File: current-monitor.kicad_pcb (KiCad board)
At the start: 4 copper layers, 70 x 60 mm, 152 parts, among them J201 CONN-3, J601 USB-MICROB, J602 SWD, J603 CONN-6, K201 RELAY-DPDT-EE2-SPLIT, K202 RELAY-DPDT-EE2-SPLIT, Q201 DRDC3105E6, U201 FSA1259A, U202 MAX4737EUD, U301 AD8429A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

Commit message: 1.0-rc1
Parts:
- added TP706: GND, libs:TESTPOINT-2.0, F.Cu at (97.4, 114.6)
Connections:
- R605 pad 1: /MCU/LED_ERROR -> /MCU/LED_CAPTURE
- R606 pad 1: /MCU/LED_CAPTURE -> /MCU/LED_CALIBRATE
- R607 pad 1: /MCU/LED_CALIBRATE -> /MCU/LED_ERROR
- U601 pad 53: /MCU/LED_CALIBRATE -> /MCU/LED_ERROR
- U601 pad 54: /MCU/LED_CAPTURE -> /MCU/LED_CALIBRATE
- U601 pad 55: /MCU/LED_ERROR -> /MCU/LED_CAPTURE
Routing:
- net /MCU/LED_ERROR: track 95.4 -> 79.2 mm
- net /MCU/LED_CAPTURE: track 86.6 -> 95.4 mm
- net /MCU/LED_CALIBRATE: track 79.2 -> 86.6 mm
- net COM: track 114.4 -> 116.1 mm, vias 107 -> 108
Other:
- board text added: "CALIBRATE"
- board text added: "CAPTURE"
- board text added: "ERROR"
- board text added: "POWER"
- board text added: "SER#"
- board text added: "v1.0"
- board text removed: "sternlabs"

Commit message: silkscreen
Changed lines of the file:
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@@
   (module libs:SMD-3225 (layer F.Cu)
     (at 142.6 115.4 180)
-    (fp_text reference C713 (at 2 0 270) (layer F.SilkS)
+    (fp_text reference C713 (at 0 -2.8 360) (layer F.SilkS)
       (effects (font (size 0.7 0.7) (thickness 0.15)))
     )
@@
     )
   )
-  (zone (net 2) (net_name COM) (layer F.SilkS) (hatch edge 0.508)
+  (zone (net 0) (net_name "") (layer F.SilkS) (hatch edge 0.508)
     (connect_pads (clearance 0.2))
     (min_thickness 0.254)

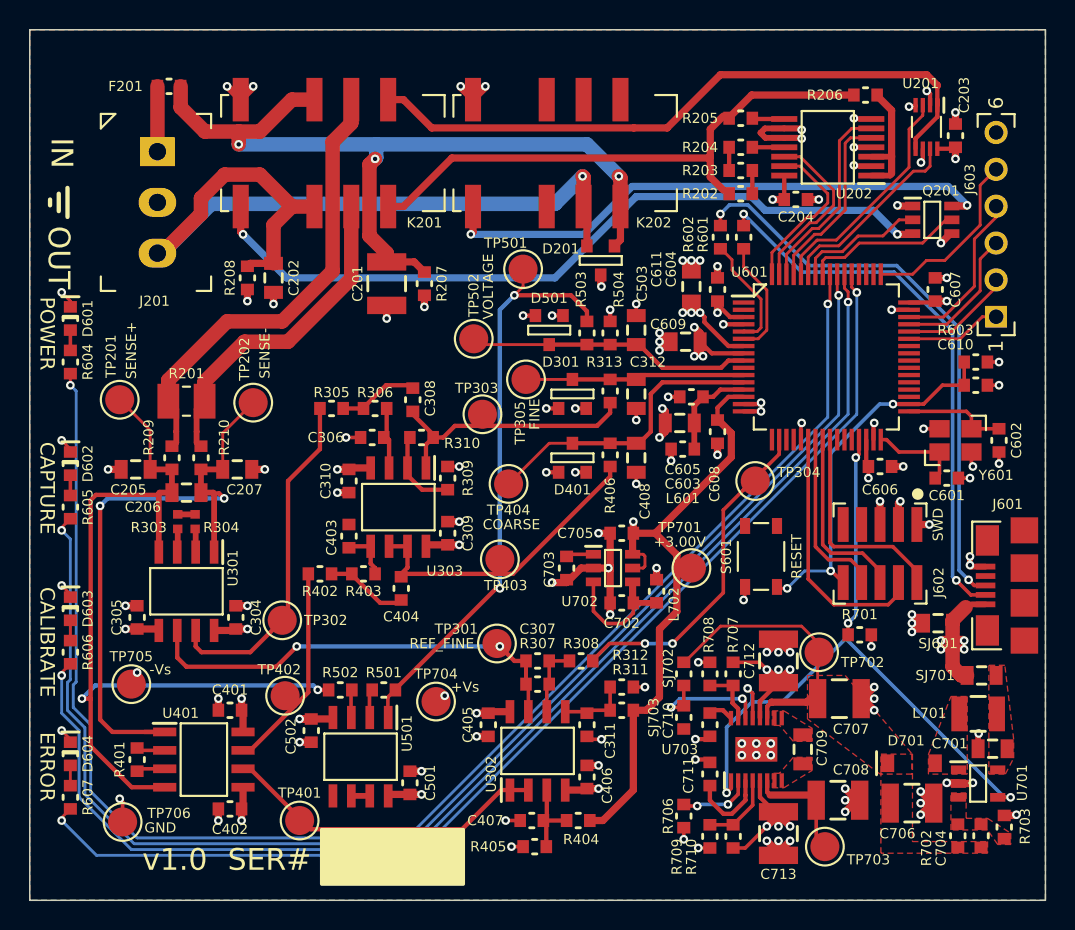
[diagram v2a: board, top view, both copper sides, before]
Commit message: move SJ for mcu
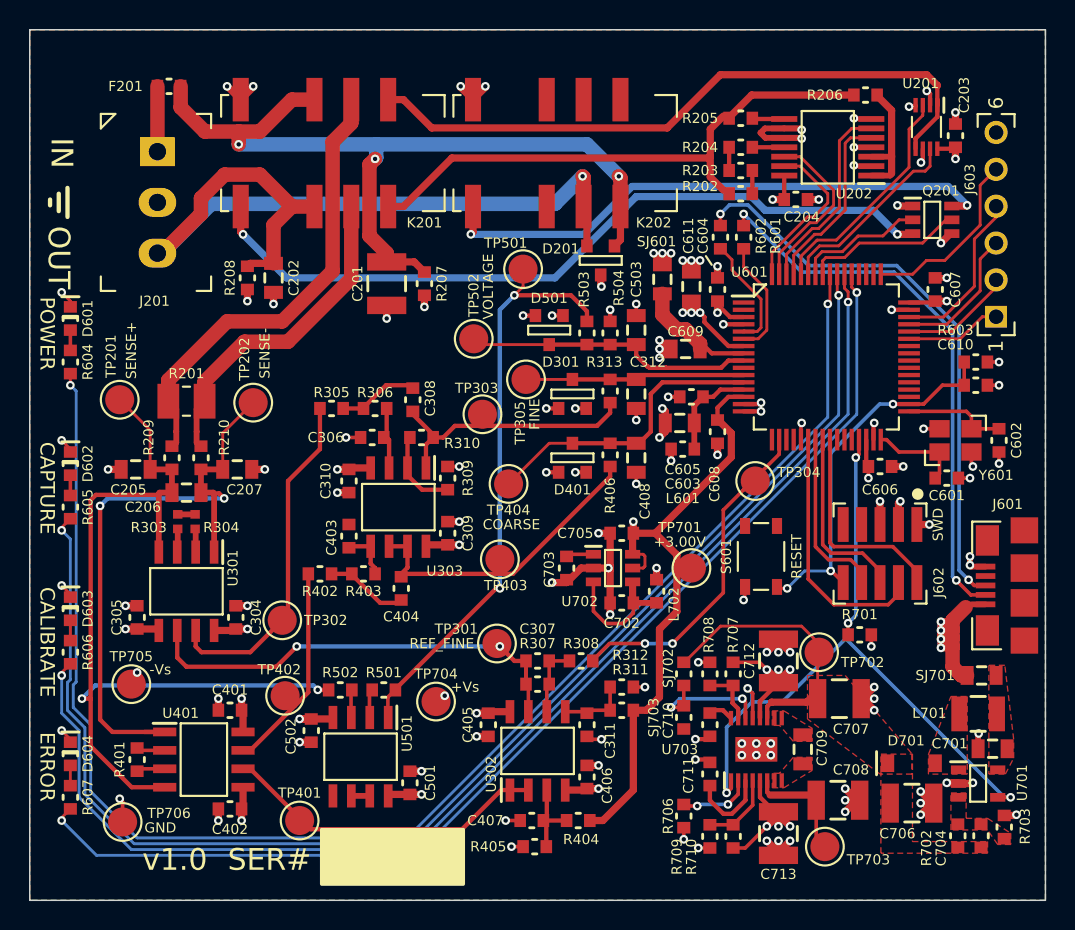
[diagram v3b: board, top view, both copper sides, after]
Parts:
- moved SJ601 30.4 mm to (134.6, 77.2), turned to 0 degrees
- moved C609 0.50 mm to (136.2, 82.0)
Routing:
- net /MCU/5V_MCU: track 34.9 -> 8.56 mm, vias 6 -> 0
- net +5V: track 39.4 -> 47.6 mm, vias 12 -> 15
- net /MCU/SENSE_VOLTAGE: track 21.9 -> 20.5 mm

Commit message: tidy up power plane
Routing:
- net -Vs: track 68.9 -> 45.2 mm
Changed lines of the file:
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@@
     (thickness 1.6)
     (drawings 20)
-    (tracks 1208)
+    (tracks 1206)
     (zones 0)
     (modules 153)
@@
     (trace_clearance 0.199)
     (zone_clearance 0.2)
-    (zone_45_only no)
+    (zone_45_only yes)
     (trace_min 0.15)
     (segment_width 0.15)
@@
   (via (at 97.6 101.3) (size 0.6) (drill 0.3) (layers F.Cu B.Cu) (net 5))
   (segment (start 108.845604 113.750999) (end 106.349001 113.750999) (width 0.5) (layer In2.Cu) (net 5))
-  (segment (start 131.650999 113.750999) (end 108.845604 113.750999) (width 0.5) (layer In2.Cu) (net 5))
   (segment (start 108.845604 113.750999) (end 108.845604 108.254396) (width 0.5) (layer In2.Cu) (net 5))
   (segment (start 108.845604 108.254396) (end 109.6 107.5) (width 0.5) (layer In2.Cu) (net 5))
-  (segment (start 132.292925 114.392925) (end 131.650999 113.750999) (width 0.5) (layer In2.Cu) (net 5))
   (segment (start 106.349001 113.750999) (end 105.6 114.5) (width 0.5) (layer In2.Cu) (net 5))
   (segment (start 141.075109 114.392925) (end 132.292925 114.392925) (width 0.5) (layer In2.Cu) (net 5))
@@
     )
   )
-  (zone (net 5) (net_name -Vs) (layer In2.Cu) (hatch edge 0.508)
+  (zone (net 2) (net_name COM) (layer In1.Cu) (hatch edge 0.508)
     (connect_pads yes (clearance 0.2))
     (min_thickness 0.254)
@@
     (polygon
       (pts
-        (xy 145.8 117.3) (xy 95.6 117.3) (xy 95.6 88.9) (xy 115.8 88.9) (xy 124.2 110.1)
-        (xy 144.4 110.1)
+        (xy 91 60) (xy 161 60) (xy 161 120) (xy 91 120)
       )
     )
   )
-  (zone (net 4) (net_name +Vs) (layer In2.Cu) (hatch edge 0.508)
-    (priority 1)
+  (zone (net 2) (net_name COM) (layer B.Cu) (hatch edge 0.508)
     (connect_pads yes (clearance 0.2))
     (min_thickness 0.254)
@@
     (polygon
       (pts
-        (xy 144.6 102.9) (xy 129 102.9) (xy 122.2 93.1) (xy 115.8 93.1) (xy 102.8 100.5)
-        (xy 103 108.1) (xy 113.2 105.3) (xy 117.2 113.5) (xy 128.4 109.7) (xy 144.6 109.9)
+        (xy 91 60) (xy 161 60) (xy 161 120) (xy 91 120)
       )
     )
   )
-  (zone (net 8) (net_name +5V) (layer In2.Cu) (hatch edge 0.508)
-    (priority 2)
-    (connect_pads yes (clearance 0.2))
+  (zone (net 0) (net_name "") (layer F.SilkS) (hatch edge 0.508)
+    (connect_pads (clearance 0.2))
     (min_thickness 0.254)
-    (fill yes (arc_segments 32) (thermal_gap 0.508) (thermal_bridge_width 0.508))
+    (fill yes (arc_segments 16) (thermal_gap 0.508) (thermal_bridge_width 0.508))
     (polygon
       (pts
-        (xy 133 95.5) (xy 133.2 100.9) (xy 155.2 104.5) (xy 160.4 98.1) (xy 160.4 62.3)
-        (xy 103.2 62.3) (xy 103 74.2) (xy 155 77.7) (xy 155 81.1) (xy 158.8 82.6)
-        (xy 154 96.3)
+        (xy 111 115) (xy 121 115) (xy 121 119) (xy 111 119)
       )
     )
   )
   (zone (net 13) (net_name +3V3) (layer In2.Cu) (hatch edge 0.508)
-    (priority 1)
+    (priority 2)
     (connect_pads yes (clearance 0.2))
     (min_thickness 0.254)
@@
     (polygon
       (pts
-        (xy 159.6 78.5) (xy 159.2 87.5) (xy 153.4 95.2) (xy 137.6 91.7) (xy 126.6 91.9)
-        (xy 123.2 77.2)
+        (xy 123 88.6) (xy 130.2 95.8) (xy 153.2 95.8) (xy 153.2 88.4) (xy 158.8 82.8)
+        (xy 155.2 79.2) (xy 155.2 77.2) (xy 124.6 77.2) (xy 123 78.8)
       )
     )
   )
-  (zone (net 2) (net_name COM) (layer In1.Cu) (hatch edge 0.508)
+  (zone (net 4) (net_name +Vs) (layer In2.Cu) (hatch edge 0.508)
+    (priority 2)
     (connect_pads yes (clearance 0.2))
     (min_thickness 0.254)
@@
     (polygon
       (pts
-        (xy 91 60) (xy 161 60) (xy 161 120) (xy 91 120)
+        (xy 127.8 101.2) (xy 144.2 101.2) (xy 144.2 108.4) (xy 124 108.4) (xy 119 113.4)
+        (xy 117 113.4) (xy 110.4 106.8) (xy 104.8 106.8) (xy 104.8 99.8) (xy 110.2 94.4)
+        (xy 121 94.4) (xy 127.8 101.2)
       )
     )
   )
-  (zone (net 2) (net_name COM) (layer B.Cu) (hatch edge 0.508)
+  (zone (net 5) (net_name -Vs) (layer In2.Cu) (hatch edge 0.508)
+    (priority 1)
     (connect_pads yes (clearance 0.2))
     (min_thickness 0.254)
@@
     (polygon
       (pts
-        (xy 91 60) (xy 161 60) (xy 161 120) (xy 91 120)
+        (xy 134.6 108.4) (xy 144.2 108.4) (xy 144.2 120) (xy 96.6 120) (xy 96.6 88.2)
+        (xy 114.4 88.2) (xy 134.6 108.4)
       )
     )
   )
-  (zone (net 0) (net_name "") (layer F.SilkS) (hatch edge 0.508)
-    (connect_pads (clearance 0.2))
+  (zone (net 8) (net_name +5V) (layer In2.Cu) (hatch edge 0.508)
+    (connect_pads yes (clearance 0.2))
     (min_thickness 0.254)
-    (fill yes (arc_segments 16) (thermal_gap 0.508) (thermal_bridge_width 0.508))
+    (fill yes (arc_segments 32) (thermal_gap 0.508) (thermal_bridge_width 0.508))
     (polygon
       (pts
-        (xy 111 115) (xy 121 115) (xy 121 119) (xy 111 119)
+        (xy 91 120) (xy 91 60) (xy 161 60) (xy 161 120)
       )
     )

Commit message: slight track cleanup
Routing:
- net Net-(K201-Pad12): track 52.8 -> 51.1 mm
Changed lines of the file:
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@@
   (segment (start 138.807125 114.037396) (end 139.39264 114.037396) (width 0.3) (layer F.Cu) (net 42))
   (segment (start 140.325109 113.104927) (end 140.325109 111.742925) (width 0.3) (layer F.Cu) (net 42) (status 20))
-  (segment (start 150.8 74.1) (end 149.149001 72.449001) (width 0.5) (layer B.Cu) (net 43))
-  (segment (start 149.149001 72.449001) (end 141.684295 72.449001) (width 0.5) (layer B.Cu) (net 43))
-  (segment (start 141.684295 72.449001) (end 140.735294 71.5) (width 0.5) (layer B.Cu) (net 43))
-  (segment (start 140.735294 71.5) (end 132.8 71.5) (width 0.5) (layer B.Cu) (net 43))
-  (segment (start 132.8 71.5) (end 127.2 77.1) (width 0.5) (layer B.Cu) (net 43))
-  (segment (start 127.2 77.1) (end 108.7 77.1) (width 0.5) (layer B.Cu) (net 43))
-  (segment (start 108.7 77.1) (end 105.7 74.1) (width 0.5) (layer B.Cu) (net 43))
+  (segment (start 150.8 74.1) (end 143.335294 74.1) (width 0.5) (layer B.Cu) (net 43))
+  (segment (start 140.735294 71.5) (end 136.488548 71.5) (width 0.5) (layer B.Cu) (net 43))
+  (segment (start 143.335294 74.1) (end 140.735294 71.5) (width 0.5) (layer B.Cu) (net 43))
+  (segment (start 136.488548 71.5) (end 132.988548 75) (width 0.5) (layer B.Cu) (net 43))
+  (segment (start 132.988548 75) (end 106.6 75) (width 0.5) (layer B.Cu) (net 43))
+  (segment (start 106.6 75) (end 105.999999 74.399999) (width 0.5) (layer B.Cu) (net 43))
+  (segment (start 105.999999 74.399999) (end 105.7 74.1) (width 0.5) (layer B.Cu) (net 43))
   (segment (start 150.8 74.1) (end 151.8 74.1) (width 0.5) (layer F.Cu) (net 43) (status 20))
   (segment (start 151.8 74.1) (end 151.85 74.05) (width 0.5) (layer F.Cu) (net 43) (status 30))
@@
   (segment (start 105.54 73.94) (end 105.7 74.1) (width 0.5) (layer F.Cu) (net 43))
   (via (at 105.7 74.1) (size 0.6) (drill 0.3) (layers F.Cu B.Cu) (net 43))
-  (segment (start 121.4 74.1) (end 129.211452 74.1) (width 0.5) (layer B.Cu) (net 44))
-  (segment (start 129.211452 74.1) (end 132.510461 70.80099) (width 0.5) (layer B.Cu) (net 44))
-  (segment (start 132.510461 70.80099) (end 154.30099 70.80099) (width 0.5) (layer B.Cu) (net 44))
   (segment (start 154.30099 70.80099) (end 155.6 72.1) (width 0.5) (layer B.Cu) (net 44))
+  (segment (start 121.4 74.1) (end 132.9 74.1) (width 0.5) (layer B.Cu) (net 44))
+  (segment (start 132.9 74.1) (end 136.19901 70.80099) (width 0.5) (layer B.Cu) (net 44))
+  (segment (start 136.19901 70.80099) (end 154.30099 70.80099) (width 0.5) (layer B.Cu) (net 44))
   (segment (start 121.55 72.183) (end 121.55 73.95) (width 0.5) (layer F.Cu) (net 44) (status 10))
   (segment (start 121.55 73.95) (end 121.4 74.1) (width 0.5) (layer F.Cu) (net 44))

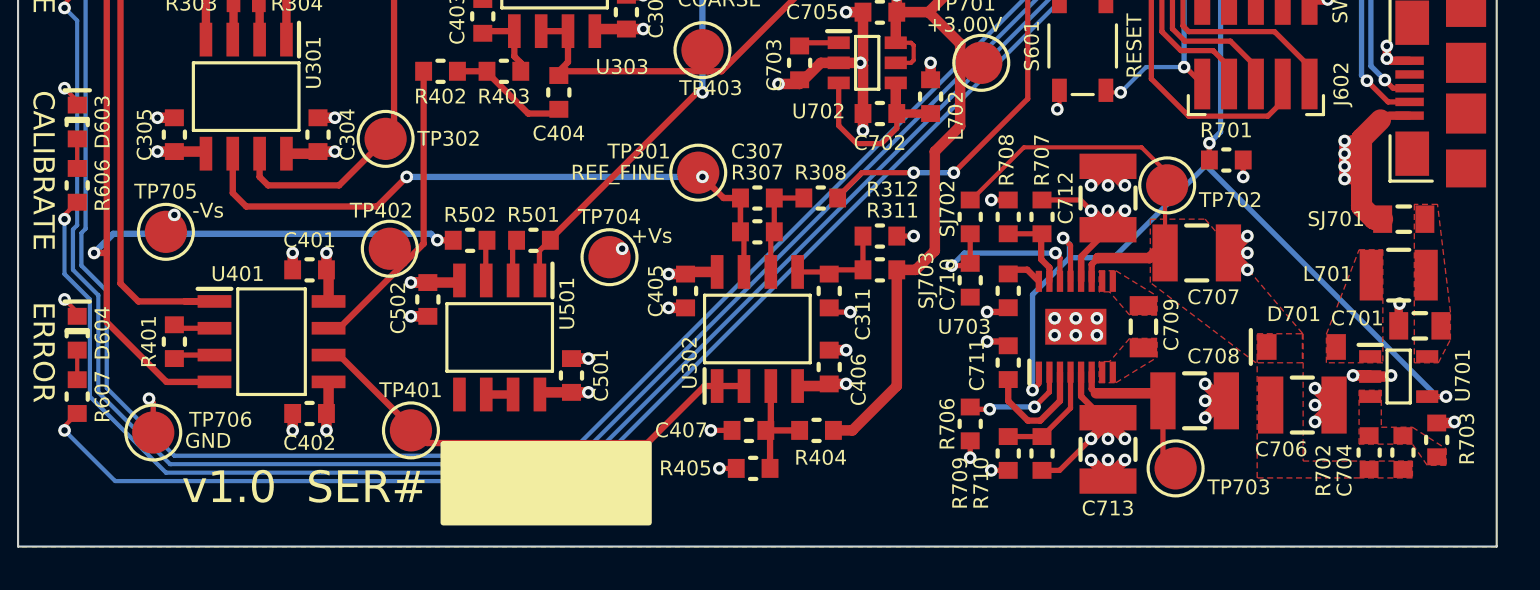
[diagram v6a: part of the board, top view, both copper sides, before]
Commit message: change power supply
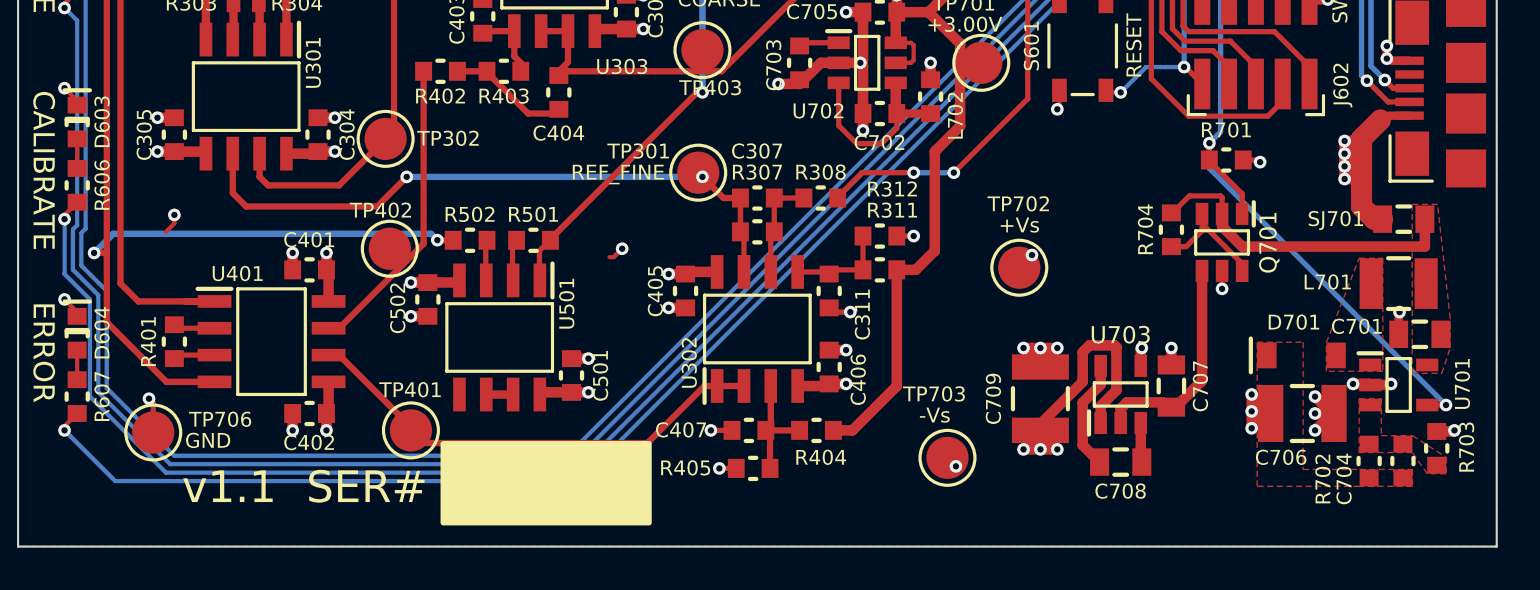
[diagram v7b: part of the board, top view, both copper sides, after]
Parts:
- removed C710, C711: 10n, libs:SMD-1608
- removed C712, C713: 10u, libs:SMD-3225
- removed R706, SJ702, SJ703: 0, libs:SMD-1608
- removed R707, R710: 1.15M, libs:SMD-1608
- removed R708, R709: 100k, libs:SMD-1608
- removed TP704: +Vs, libs:TESTPOINT-2.0
- removed TP705: -Vs, libs:TESTPOINT-2.0
- added Q701: DMG6601LVT, libs:SOT-23-6, F.Cu at (148.0, 105.6)
- added R704: 51k, libs:SMD-1608, F.Cu at (145.6, 105.0)
- C704: value 120p -> 134p
- C707, C708: value 10u -> 2.2u; footprint libs:SMD-3225 -> libs:SMD-2012
- C709: value 2.2u -> 10u; footprint libs:SMD-2012 -> libs:SMD-3225
- R702: value 174k -> 149k
- TP702: value +Vs_UNREG -> +Vs
- TP703: value -Vs_UNREG -> -Vs
- U703: value LTC3260MSE -> TPS6040x; footprint libs:MSOP-16-EP -> libs:SOT-23-5
- moved TP703 10.8 mm to (135.0, 115.8)
- moved TP702 8.01 mm to (138.4, 106.8)
- moved C707 6.41 mm to (145.6, 112.4), turned to 180 degrees
- moved C709 5.95 mm to (139.4, 113.0), turned to 180 degrees
- moved C708 4.55 mm to (143.2, 116.0), turned to 270 degrees
- moved U703 3.85 mm to (143.2, 112.8)
- moved C701 0.40 mm to (157.4, 110.0)
- moved C704 0.40 mm to (156.6, 116.0)
- moved C706 0.40 mm to (151.8, 113.7)
- moved D701 0.40 mm to (151.8, 111.0)
- moved R702 0.40 mm to (155.0, 116.0)
- moved L701 0.40 mm to (156.4, 107.6)
- moved R703 0.40 mm to (158.2, 115.4)
- moved U701 0.40 mm to (156.4, 112.4)
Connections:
- C704 pad 1: /Power Supply/+Vs_UNREG -> +Vs
- C706 pad 1: /Power Supply/+Vs_UNREG -> +Vs
- C707 pad 1: /Power Supply/+Vs_UNREG -> Net-(C707-Pad1)
- C708 pad 1: /Power Supply/-Vs_UNREG -> Net-(C708-Pad1)
- C708 pad 2: COM -> Net-(C708-Pad2)
- C709 pad 1: /Power Supply/PUMP+ -> -Vs
- C709 pad 2: /Power Supply/PUMP- -> COM
- D701 pad C: /Power Supply/+Vs_UNREG -> +Vs
- R702 pad 1: /Power Supply/+Vs_UNREG -> +Vs
- TP702 pad TP: /Power Supply/+Vs_UNREG -> +Vs
- TP703 pad TP: /Power Supply/-Vs_UNREG -> -Vs
- U703 pad 1: /MCU/VS_ENABLE -> -Vs
- U703 pad 2: Net-(R706-Pad1) -> Net-(C707-Pad1)
- U703 pad 3: Net-(C711-Pad2) -> Net-(C708-Pad1)
- U703 pad 4: Net-(R709-Pad2) -> COM
- U703 pad 5: -Vs -> Net-(C708-Pad2)
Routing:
- net /Power Supply/+Vs_UNREG: track 19.1 -> 0.00 mm
- net COM: track 116.2 -> 99.1 mm, vias 108 -> 91
- net /MCU/VS_ENABLE: track 51.2 -> 34.9 mm, vias 5 -> 3
- net /Power Supply/5V_ANALOG: track 0.09 -> 15.5 mm
- net Net-(C707-Pad1): track 0.00 -> 10.5 mm
- net Net-(SJ702-Pad1): track 8.90 -> 0.00 mm, vias 2 -> 0
- net /Power Supply/-Vs_UNREG: track 7.90 -> 0.00 mm
- net Net-(Q701-Pad3): track 0.00 -> 6.05 mm
- net Net-(C711-Pad2): track 5.40 -> 0.00 mm
- net Net-(R709-Pad2): track 5.28 -> 0.00 mm
- net Net-(C708-Pad2): track 0.00 -> 5.23 mm
- net Net-(R706-Pad1): track 5.20 -> 0.00 mm, vias 2 -> 0
- net -Vs: track 45.2 -> 49.9 mm
- net +Vs: track 83.8 -> 79.2 mm
- net Net-(R707-Pad2): track 4.10 -> 0.00 mm
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- added copper zone on F.Cu, net +Vs
- removed copper zone on F.Cu, net /Power Supply/+Vs_UNREG
- removed copper zone on F.Cu, net /Power Supply/PUMP+
- removed copper zone on F.Cu, net /Power Supply/PUMP-
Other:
- board text added: "v1.1"
- board text removed: "v1.0"

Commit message: pcb cleanup
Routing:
- net (no net): track 1.73 -> 0.97 mm, vias 2 -> 1
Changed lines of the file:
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@@
     (links 311)
     (no_connects 0)
-    (area 90.949999 59.949999 161.050001 120.050001)
+    (area 90.949999 59.949999 162.774001 120.050001)
     (thickness 1.6)
     (drawings 20)
-    (tracks 1140)
+    (tracks 1136)
     (zones 0)
     (modules 142)
@@
   (gr_line (start 91 120) (end 161 120) (layer Edge.Cuts) (width 0.1))
   (gr_line (start 161 60) (end 161 120) (layer Edge.Cuts) (width 0.1))
-  (segment (start 119.300003 106.199999) (end 119.600002 105.9) (width 0.2) (layer F.Cu) (net 0) (status 30))
-  (segment (start 119.200002 106.3) (end 119.300003 106.199999) (width 0.2) (layer F.Cu) (net 0) (status 30))
-  (segment (start 119 106.3) (end 119.200002 106.3) (width 0.2) (layer F.Cu) (net 0) (status 30))
-  (via (at 119.600002 105.9) (size 0.6) (drill 0.3) (layers F.Cu B.Cu) (net 0) (status 30))
   (segment (start 98.4 104.3) (end 98.4 104.7) (width 0.2) (layer F.Cu) (net 0) (status 30))
   (via (at 98.4 104.3) (size 0.6) (drill 0.3) (layers F.Cu B.Cu) (net 0) (status 30))
